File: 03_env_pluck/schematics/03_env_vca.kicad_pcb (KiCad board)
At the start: 2 copper layers, 20 x 109 mm, 45 parts, among them J1 gate in, J2 signal in, J3 Eurorack, J4 Signal out, J5 env out, Q1 BC847, Q2 BC847, SW1 Pluck / AD 1, U1 TL072, U2 LM358

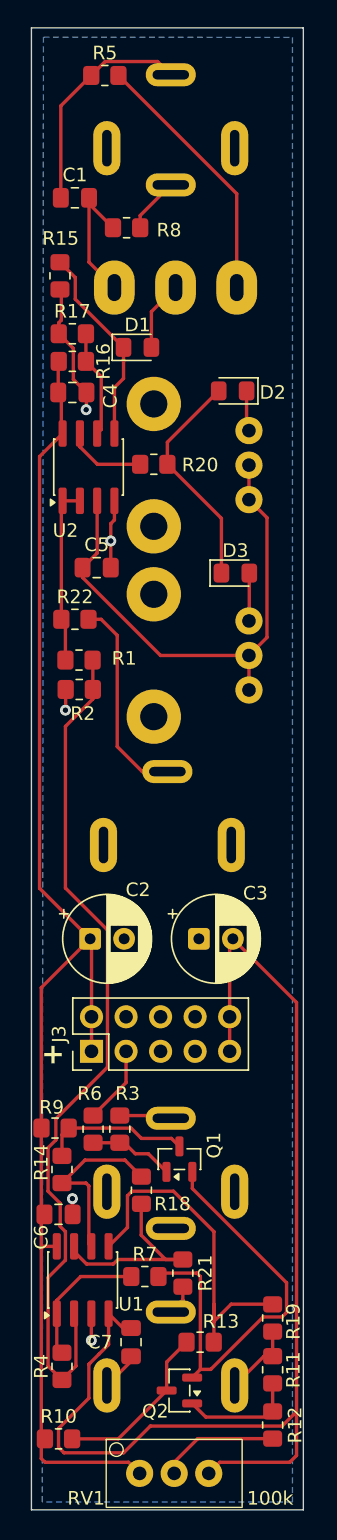
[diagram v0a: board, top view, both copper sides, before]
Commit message: added 3d models
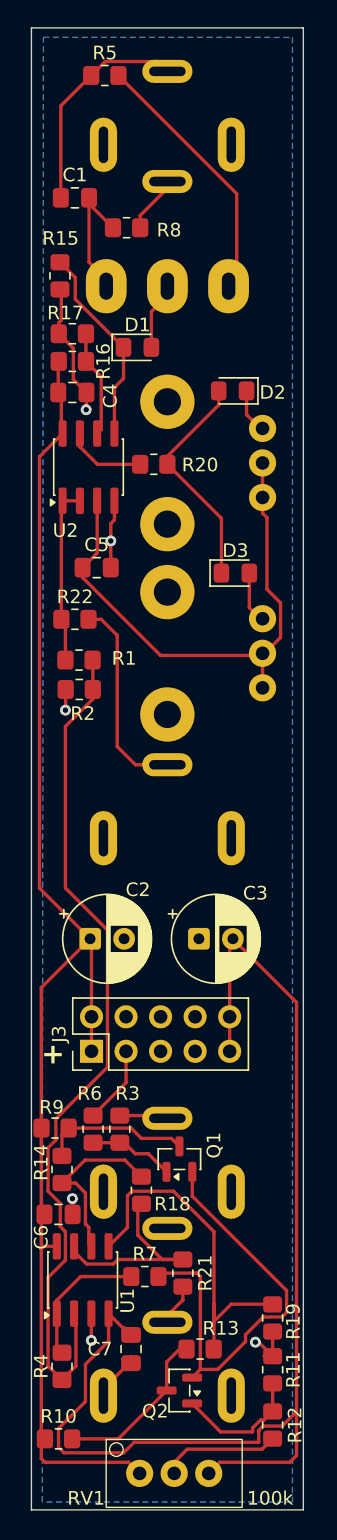
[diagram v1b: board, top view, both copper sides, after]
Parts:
- moved RV2 1.01 mm to (10.0, 32.0)
- moved RV3 1.01 mm to (10.0, 46.0)
- moved J4 0.79 mm to (10.0, 100.0)
- moved SW1 0.61 mm to (10.0, 19.0)
- moved C7 0.51 mm to (7.33, 97.2)
- moved R13 0.51 mm to (12.4, 97.2)
- moved J5 0.50 mm to (10.0, 59.0)
- moved J1 0.35 mm to (10.0, 8.00)
- moved J2 0.25 mm to (10.0, 85.0)
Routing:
- net GND: track 37.4 -> 36.1 mm, vias 5 -> 6
- net Net-(Q2-B): track 8.57 -> 9.63 mm
- net Net-(U2A-+): track 38.3 -> 39.3 mm
- net -12V: track 87.7 -> 88.4 mm

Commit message: 3d modules for 03
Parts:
- J4, J5: footprint cynthia:3.5mm jack mono -> cynthia:3.5mm jack mono switched
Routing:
- net GND: track 36.1 -> 38.0 mm, vias 6 -> 5
- net -12V: track 88.4 -> 89.9 mm
